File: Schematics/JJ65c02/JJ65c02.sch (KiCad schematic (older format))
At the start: 20 parts

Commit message: Updates w/ latest schematic
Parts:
- removed R2: 3.7K, Resistor_THT:R_Axial_DIN0207_L6.3mm_D2.5mm_P7.62mm_Horizontal, symbol Device:R
- RV1: symbol Device:R_POT_TRIM -> Device:R_POT
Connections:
- net labels added: A~IRQ, V~IRQ
- wire segments 259 -> 253

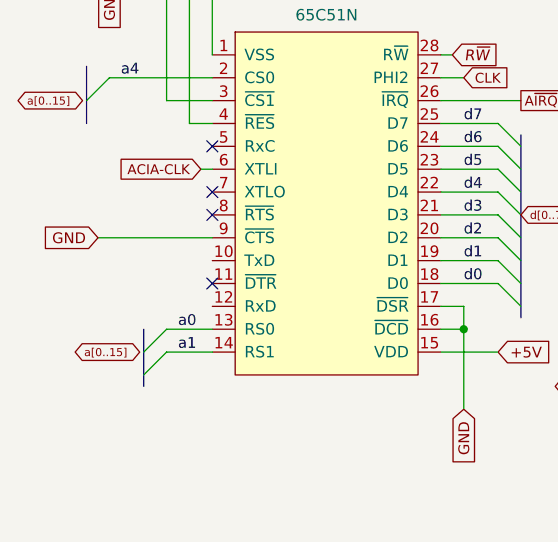
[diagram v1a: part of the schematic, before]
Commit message: Add in max232 board
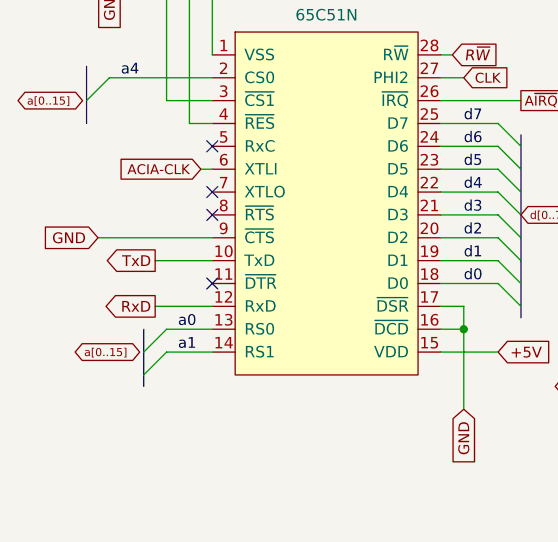
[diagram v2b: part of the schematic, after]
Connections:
- net TxD: now reaches ACIA1.10 (TxD)
- net RxD: now reaches ACIA1.12 (RxD)
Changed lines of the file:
@@
 Wire Wire Line
 	6300 4800 5900 4800
+Text GLabel 1150 5850 0    47   Output ~ 0
+TxD
+Text GLabel 1150 6050 0    47   Output ~ 0
+RxD
+Wire Wire Line
+	1400 5850 1150 5850
+Wire Wire Line
+	1150 6050 1400 6050
 Wire Bus Line
 	5150 3050 5150 3250

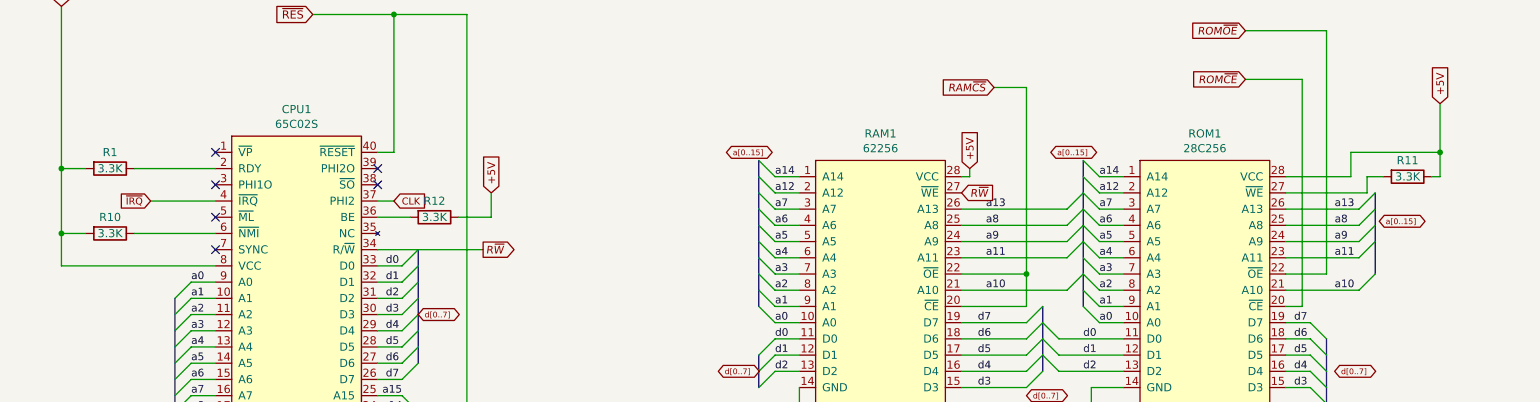
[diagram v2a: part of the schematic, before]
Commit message: Update w/ latest schematics and datasheets. Fully on-board memory map and restart ckt
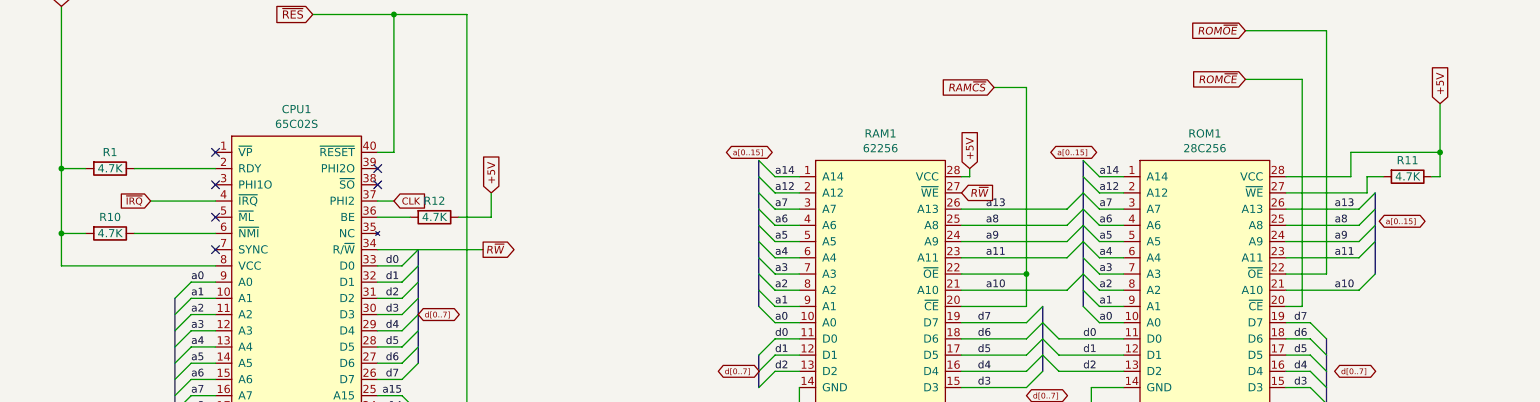
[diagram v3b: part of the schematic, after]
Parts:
- R1, R10, R11, R12: value 3.3K -> 4.7K
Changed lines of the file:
@@
 P 1150 1900
 F 0 "R1" V 1050 1900 50  0000 C CNN
-F 1 "3.3K" V 1150 1900 50  0000 C CNN
+F 1 "4.7K" V 1150 1900 50  0000 C CNN
 F 2 "Resistor_THT:R_Axial_DIN0207_L6.3mm_D2.5mm_P7.62mm_Horizontal" H 1150 1900 50  0001 C CNN
 F 3 "~" H 1150 1900 50  0001 C CNN
@@
 P 1150 2300
 F 0 "R10" V 1050 2300 50  0000 C CNN
-F 1 "3.3K" V 1150 2300 50  0000 C CNN
+F 1 "4.7K" V 1150 2300 50  0000 C CNN
 F 2 "Resistor_THT:R_Axial_DIN0207_L6.3mm_D2.5mm_P7.62mm_Horizontal" H 1150 2300 50  0001 C CNN
 F 3 "~" H 1150 2300 50  0001 C CNN
@@
 P 9150 1950
 F 0 "R11" V 9050 1950 50  0000 C CNN
-F 1 "3.3K" V 9150 1950 50  0000 C CNN
+F 1 "4.7K" V 9150 1950 50  0000 C CNN
 F 2 "Resistor_THT:R_Axial_DIN0207_L6.3mm_D2.5mm_P7.62mm_Horizontal" H 9150 1950 50  0001 C CNN
 F 3 "~" H 9150 1950 50  0001 C CNN
@@
 P 3150 2200
 F 0 "R12" V 3050 2200 50  0000 C CNN
-F 1 "3.3K" V 3150 2200 50  0000 C CNN
+F 1 "4.7K" V 3150 2200 50  0000 C CNN
 F 2 "Resistor_THT:R_Axial_DIN0207_L6.3mm_D2.5mm_P7.62mm_Horizontal" H 3150 2200 50  0001 C CNN
 F 3 "~" H 3150 2200 50  0001 C CNN

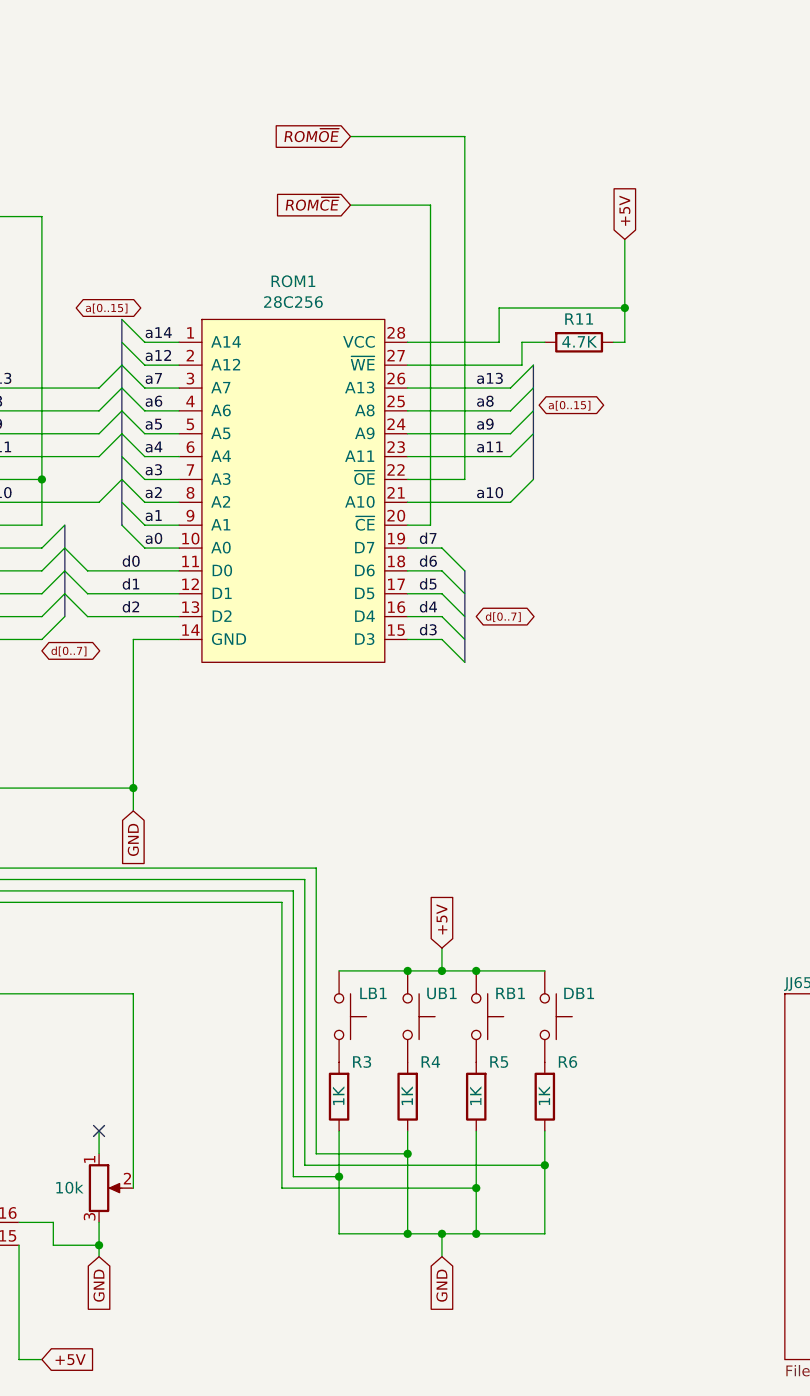
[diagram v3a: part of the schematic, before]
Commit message: Update schematics: pull down ckt was incorrect
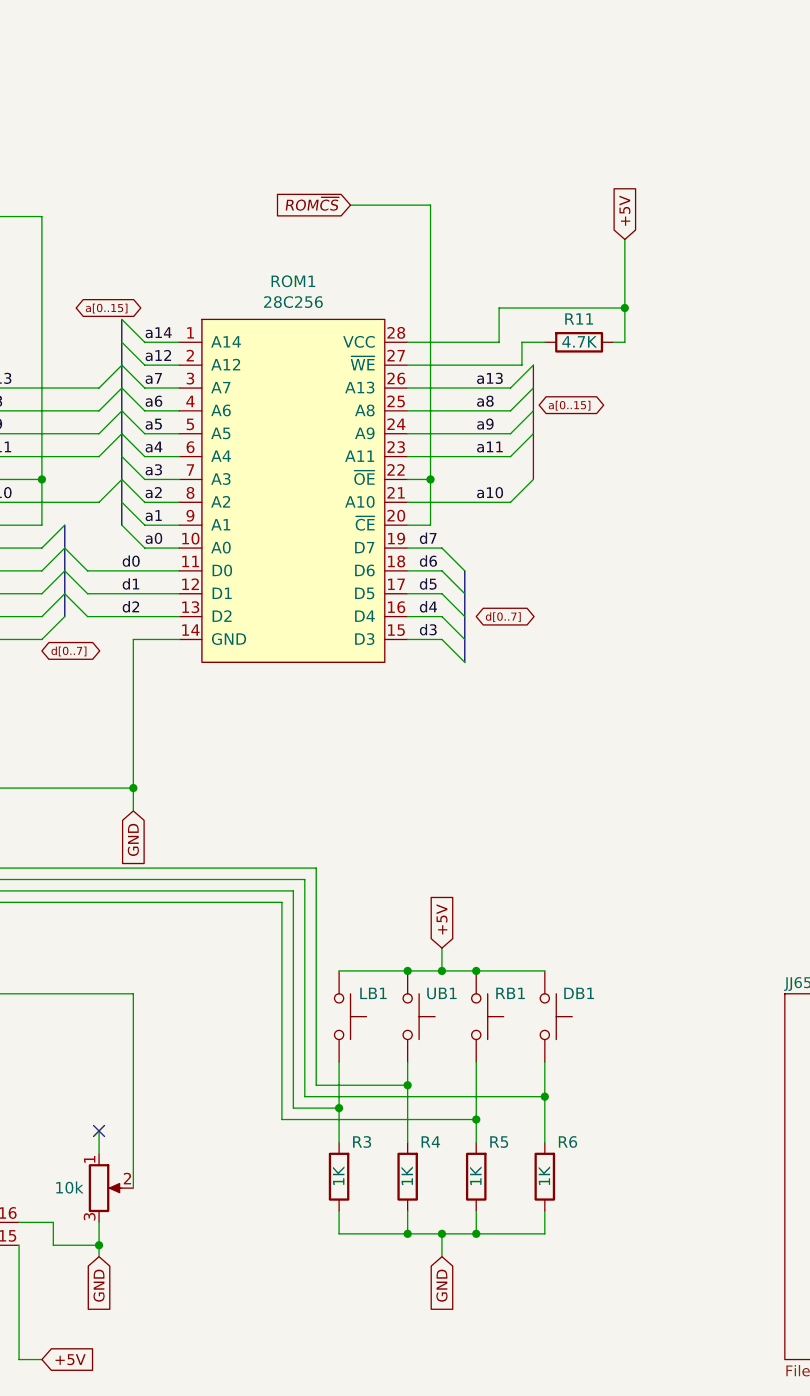
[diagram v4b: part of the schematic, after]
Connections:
- net ROM~OE is gone; now on net ROM~CS: ROM1.22 (~OE)
- net GND: no longer VIA1.3 (PA1), VIA1.4 (PA2), VIA1.5 (PA3), VIA1.6 (PA4)
- net at LB1.2, R3.2: now also VIA1.5 (PA3)
- net at R4.2, UB1.2: now also VIA1.3 (PA1)
- net at R5.2, RB1.2: now also VIA1.6 (PA4)
- net at DB1.2, R6.2: now also VIA1.4 (PA2)
- net ROM~CE renamed ROM~CS
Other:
- moved on the sheet: R3, R4, R5, R6
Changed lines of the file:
@@
 	6800 2550 6800 2750
-Wire Wire Line
-	8650 2550 8400 2550
 Wire Wire Line
 	2800 1800 2900 1800
@@
 L Device:R R6
 U 1 1 613C0CBF
-P 9000 5250
-F 0 "R6" H 8900 5100 50  0000 C CNN
-F 1 "1K" V 9000 5250 50  0000 C CNN
-F 2 "Resistor_THT:R_Axial_DIN0207_L6.3mm_D2.5mm_P7.62mm_Horizontal" H 9000 5250 50  0001 C CNN
-F 3 "~" H 9000 5250 50  0001 C CNN
-	1    9000 5250
+P 9000 5600
+F 0 "R6" H 8900 5450 50  0000 C CNN
+F 1 "1K" V 9000 5600 50  0000 C CNN
+F 2 "Resistor_THT:R_Axial_DIN0207_L6.3mm_D2.5mm_P7.62mm_Horizontal" H 9000 5600 50  0001 C CNN
+F 3 "~" H 9000 5600 50  0001 C CNN
+	1    9000 5600
 	-1   0    0    1
 $EndComp
@@
 L Device:R R5
 U 1 1 613C09A0
-P 8700 5250
-F 0 "R5" H 8600 5100 50  0000 C CNN
-F 1 "1K" V 8700 5250 50  0000 C CNN
-F 2 "Resistor_THT:R_Axial_DIN0207_L6.3mm_D2.5mm_P7.62mm_Horizontal" H 8700 5250 50  0001 C CNN
-F 3 "~" H 8700 5250 50  0001 C CNN
-	1    8700 5250
+P 8700 5600
+F 0 "R5" H 8600 5450 50  0000 C CNN
+F 1 "1K" V 8700 5600 50  0000 C CNN
+F 2 "Resistor_THT:R_Axial_DIN0207_L6.3mm_D2.5mm_P7.62mm_Horizontal" H 8700 5600 50  0001 C CNN
+F 3 "~" H 8700 5600 50  0001 C CNN
+	1    8700 5600
 	-1   0    0    1
 $EndComp
@@
 L Device:R R4
 U 1 1 613C0477
-P 8400 5250
-F 0 "R4" H 8300 5100 50  0000 C CNN
-F 1 "1K" V 8400 5250 50  0000 C CNN
-F 2 "Resistor_THT:R_Axial_DIN0207_L6.3mm_D2.5mm_P7.62mm_Horizontal" H 8400 5250 50  0001 C CNN
-F 3 "~" H 8400 5250 50  0001 C CNN
-	1    8400 5250
+P 8400 5600
+F 0 "R4" H 8300 5450 50  0000 C CNN
+F 1 "1K" V 8400 5600 50  0000 C CNN
+F 2 "Resistor_THT:R_Axial_DIN0207_L6.3mm_D2.5mm_P7.62mm_Horizontal" H 8400 5600 50  0001 C CNN
+F 3 "~" H 8400 5600 50  0001 C CNN
+	1    8400 5600
 	-1   0    0    1
 $EndComp
@@
 L Device:R R3
 U 1 1 613AF256
-P 8100 5250
-F 0 "R3" H 8000 5100 50  0000 C CNN
-F 1 "1K" V 8100 5250 50  0000 C CNN
-F 2 "Resistor_THT:R_Axial_DIN0207_L6.3mm_D2.5mm_P7.62mm_Horizontal" H 8100 5250 50  0001 C CNN
-F 3 "~" H 8100 5250 50  0001 C CNN
-	1    8100 5250
+P 8100 5600
+F 0 "R3" H 8000 5450 50  0000 C CNN
+F 1 "1K" V 8100 5600 50  0000 C CNN
+F 2 "Resistor_THT:R_Axial_DIN0207_L6.3mm_D2.5mm_P7.62mm_Horizontal" H 8100 5600 50  0001 C CNN
+F 3 "~" H 8100 5600 50  0001 C CNN
+	1    8100 5600
 	-1   0    0    1
 $EndComp
@@
 	8550 4700 8400 4700
 Wire Wire Line
-	8700 5400 8700 5650
-Wire Wire Line
-	8400 5400 8400 5500
-Wire Wire Line
 	4700 4900 5000 4900
 Wire Wire Line
@@
 Wire Wire Line
 	5050 5000 5050 4350
-Wire Wire Line
-	8000 4250 8000 5500
-Wire Wire Line
-	8000 5500 8400 5500
-Connection ~ 8400 5500
-Wire Wire Line
-	8400 5500 8400 5850
-Wire Wire Line
-	7950 4300 7950 5550
-Wire Wire Line
-	7900 4350 7900 5600
-Wire Wire Line
-	7850 4400 7850 5650
-Wire Wire Line
-	7850 5650 8700 5650
-Connection ~ 8700 5650
-Wire Wire Line
-	8700 5650 8700 5850
-Wire Wire Line
-	9000 5400 9000 5550
-Wire Wire Line
-	8100 5400 8100 5600
-Wire Wire Line
-	7950 5550 9000 5550
-Connection ~ 9000 5550
-Wire Wire Line
-	9000 5550 9000 5850
-Wire Wire Line
-	7900 5600 8100 5600
-Connection ~ 8100 5600
-Wire Wire Line
-	8100 5600 8100 5850
 Wire Wire Line
 	4700 5500 5250 5500
@@
 Text GLabel 5250 6350 2    35   BiDi ~ 0
 pb[0..7]
-Wire Wire Line
-	8100 5850 8400 5850
-Connection ~ 8400 5850
-Wire Wire Line
-	8400 5850 8550 5850
 Connection ~ 8550 5850
-Wire Wire Line
-	8550 5850 8700 5850
-Connection ~ 8700 5850
-Wire Wire Line
-	8700 5850 9000 5850
 Wire Wire Line
 	7200 3900 7200 4000
@@
 RAM~CS
 Text GLabel 8150 1350 0    47   Input Italic 0
-ROM~CE
-Text GLabel 8150 1050 0    47   Input Italic 0
-ROM~OE
+ROM~CS
 Wire Wire Line
 	6800 1400 6800 2550
 Wire Wire Line
-	8650 1050 8650 2550
-Wire Wire Line
-	8650 1050 8150 1050
-Wire Wire Line
-	8500 2750 8500 1350
+	8500 2750 8500 2550
 Wire Wire Line
 	8500 1350 8150 1350
@@
 Wire Wire Line
 	1150 6050 1400 6050
+Wire Wire Line
+	8400 2550 8500 2550
+Connection ~ 8500 2550
+Wire Wire Line
+	8500 2550 8500 1350
+Wire Wire Line
+	8550 5850 8700 5850
+Wire Wire Line
+	8100 5850 8400 5850
+Wire Wire Line
+	8100 5850 8100 5750
+Wire Wire Line
+	8400 5750 8400 5850
+Connection ~ 8400 5850
+Wire Wire Line
+	8400 5850 8550 5850
+Wire Wire Line
+	8700 5750 8700 5850
+Connection ~ 8700 5850
+Wire Wire Line
+	8700 5850 9000 5850
+Wire Wire Line
+	9000 5750 9000 5850
+Wire Wire Line
+	8100 5100 8100 5300
+Wire Wire Line
+	8400 5100 8400 5200
+Wire Wire Line
+	8700 5100 8700 5350
+Wire Wire Line
+	9000 5100 9000 5250
+Wire Wire Line
+	8000 4250 8000 5200
+Wire Wire Line
+	8000 5200 8400 5200
+Connection ~ 8400 5200
+Wire Wire Line
+	8400 5200 8400 5450
+Wire Wire Line
+	7950 4300 7950 5250
+Wire Wire Line
+	7950 5250 9000 5250
+Connection ~ 9000 5250
+Wire Wire Line
+	9000 5250 9000 5450
+Wire Wire Line
+	7900 4350 7900 5300
+Wire Wire Line
+	7900 5300 8100 5300
+Connection ~ 8100 5300
+Wire Wire Line
+	8100 5300 8100 5450
+Wire Wire Line
+	7850 4400 7850 5350
+Wire Wire Line
+	7850 5350 8700 5350
 Wire Bus Line
 	5150 3050 5150 3250
@@
 Wire Bus Line
 	1550 2700 1550 4100
+Connection ~ 8700 5350
+Wire Wire Line
+	8700 5350 8700 5450
 $EndSCHEMATC

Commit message: Add in basic sound capability
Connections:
- net SND_IN: now reaches VIA1.19 (CB2)
- no-connect marks 16 -> 15
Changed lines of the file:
@@
 	3550 5150 3350 5150
 NoConn ~ 4700 6300
-NoConn ~ 4700 6400
 Entry Wire Line
 	3200 6400 3300 6300
@@
 Wire Wire Line
 	8700 5350 8700 5450
+Text GLabel 4900 6400 2    47   Output ~ 0
+SND_IN
+Wire Wire Line
+	4900 6400 4700 6400
 Wire Bus Line
 	5150 3050 5150 3250

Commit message: PCB work
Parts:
- added R10, R9: 4.7K, Resistor_THT:R_Axial_DIN0207_L6.3mm_D2.5mm_P7.62mm_Horizontal, symbol Device:R
- added U1: 74HC08, Package_DIP:DIP-14_W7.62mm_Socket, symbol 74xx:74LS08
- DB1, LB1, RB1, UB1: footprint Button_Switch_THT:SW_PUSH_6mm_H4.3mm -> Button_Switch_THT:SW_PUSH_6mm
- LEDDisplay1: footprint Display:WC1602A -> JJ65c02:LCD-20x4v2
- ROM1: footprint Package_DIP:DIP-28_W15.24mm_Socket -> Socket:DIP_Socket-28_W11.9_W12.7_W15.24_W17.78_W18.5_3M_228-1277-00-0602J
- renumbered R10 to R2, R12 to R3, R3 to R4, R11 to R5, R4 to R6, R5 to R7, R6 to R8
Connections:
- net +5V: now also R10.2, R9.1, U1.14 (VCC)
- net A~IRQ: now also R10.1, U1.2
- net GND: now also U1.12, U1.13, U1.7 (GND)
- net ~IRQ: now also U1.8
- net V~IRQ renamed V1~IRQ
- net V1~IRQ: now also U1.1
- new net: U1.10, U1.3
- new net: R9.2, U1.4
- new net: U1.6, U1.9
- new net V2~IRQ: U1.5
- no-connect marks 15 -> 16
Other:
- note added: "~IRQ~ Logic Glue"
- moved on the sheet: R5, RAM1, ROM1
